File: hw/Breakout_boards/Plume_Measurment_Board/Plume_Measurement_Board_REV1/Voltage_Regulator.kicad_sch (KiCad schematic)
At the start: 0 parts

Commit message: Added Micro-Lock Connectors
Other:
- note added: "5V Voltage Regulator"
- note added: "LMP7721"
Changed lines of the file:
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@@
 	(generator_version "10.0")
 	(paper "A4")
+	(rectangle
+		(start 15.24 15.24)
+		(end 143.51 106.68)
+		(stroke
+			(width 0)
+			(type dash)
+		)
+		(fill
+			(type none)
+		)
+	)
+	(text "LMP7721\n"
+		(exclude_from_sim no)
+		(at 25.0662 22.5284 0)
+		(effects
+			(font
+				(size 2.286 2.286)
+			)
+		)
+	)
+	(text "5V Voltage Regulator"
+		(exclude_from_sim no)
+		(at 17.018 19.812 0)
+		(effects
+			(font
+				(size 2 2)
+				(thickness 0.4)
+				(bold yes)
+			)
+			(justify left bottom)
+		)
+	)
 )

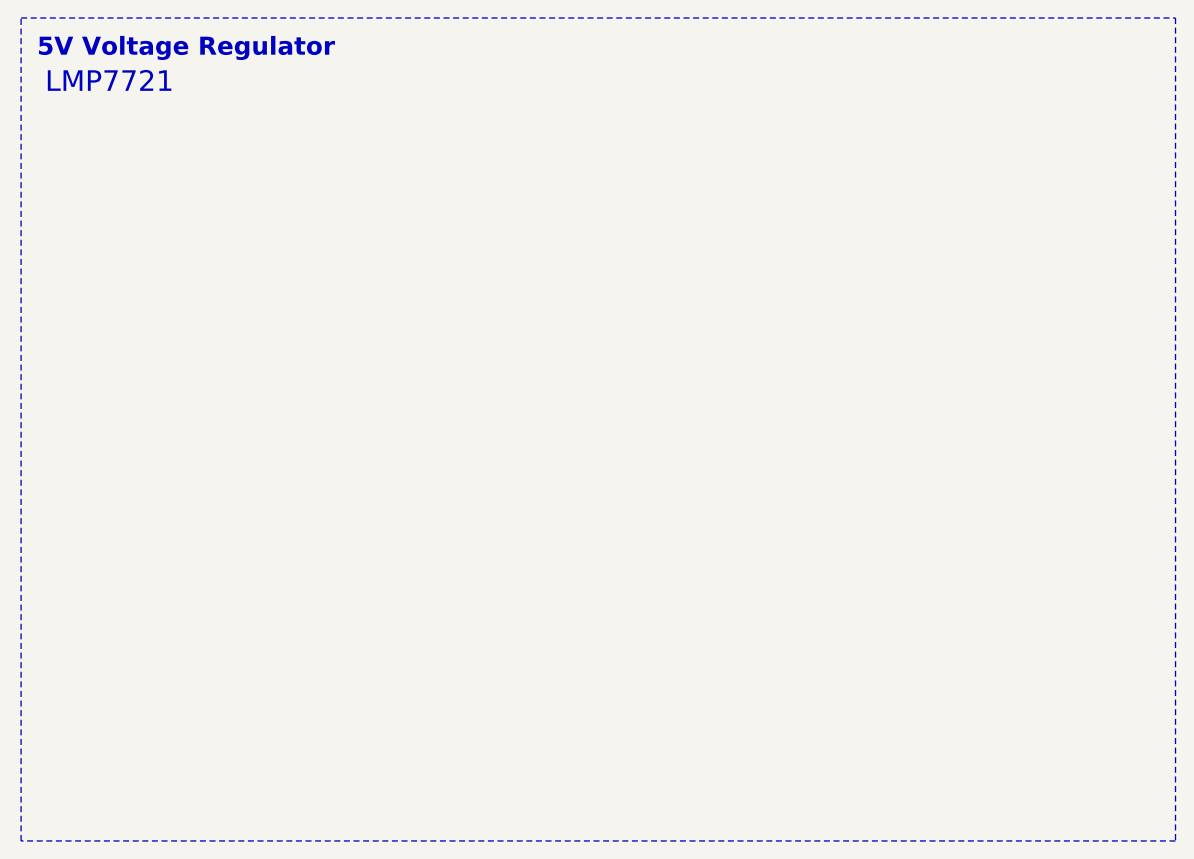
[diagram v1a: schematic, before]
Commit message: Voltage Regulator Library Import + Connector Additions
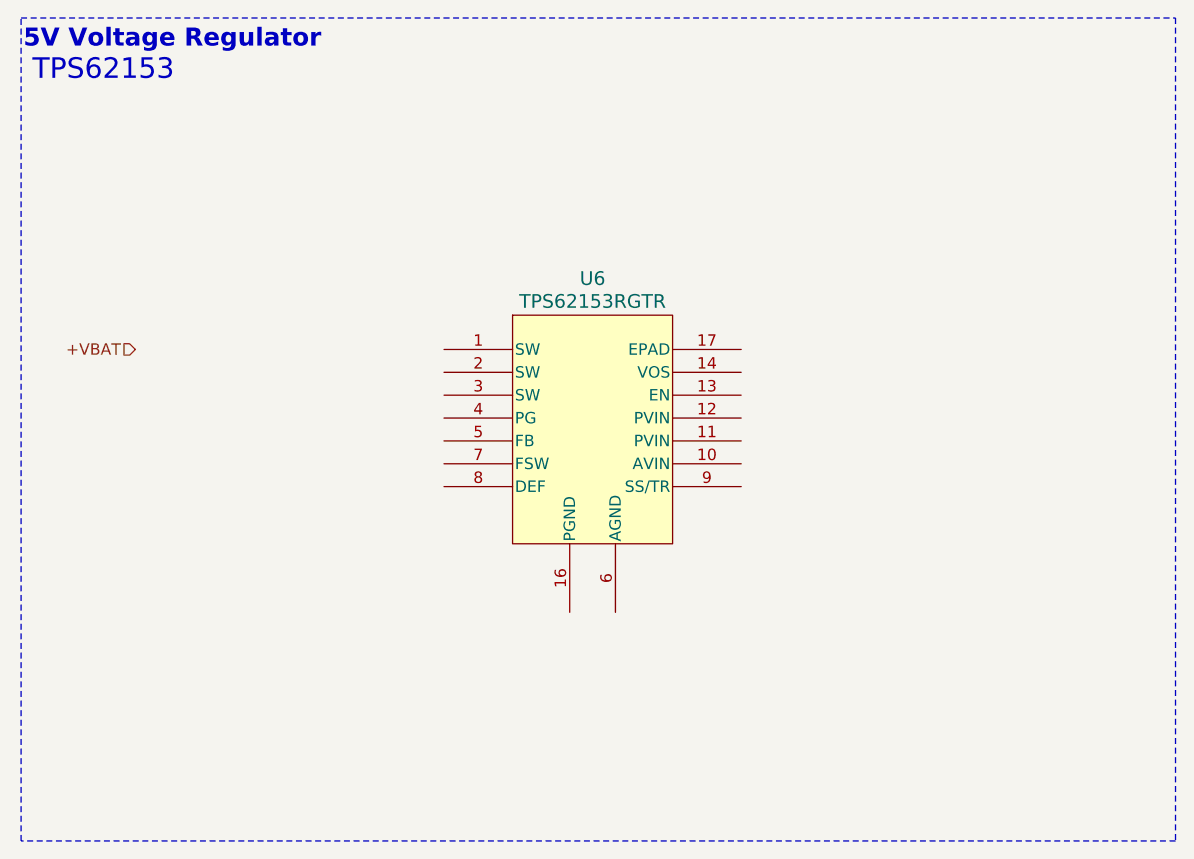
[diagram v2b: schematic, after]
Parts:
- added U6: TPS62153RGTR, RGT16_1P7X1P7, symbol Voltage_Regulator_Texas_Instruments:TPS62153RGTR
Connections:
- new net: U6.15 (PGND), U6.16 (PGND)
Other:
- note added: "TPS62153"
- note removed: "LMP7721"
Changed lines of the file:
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@@
 		)
 	)
-	(text "LMP7721\n"
+	(text "TPS62153\n"
 		(exclude_from_sim no)
-		(at 25.0662 22.5284 0)
+		(at 24.384 21.082 0)
 		(effects
 			(font
@@
 	(text "5V Voltage Regulator"
 		(exclude_from_sim no)
-		(at 17.018 19.812 0)
+		(at 15.494 18.796 0)
 		(effects
 			(font
@@
 		)
 	)
+	(hierarchical_label "+VBAT"
+		(shape input)
+		(at 27.94 52.07 180)
+		(effects
+			(font
+				(size 1.27 1.27)
+			)
+			(justify right)
+		)
+	)
+	(symbol
+		(lib_id "Voltage_Regulator_Texas_Instruments:TPS62153RGTR")
+		(at 48.26 50.8 0)
+		(unit 1)
+		(body_style 1)
+		(exclude_from_sim no)
+		(in_bom yes)
+		(on_board yes)
+		(in_pos_files yes)
+		(dnp no)
+		(property "Reference" "U6"
+			(at 78.74 44.196 0)
+			(show_name no)
+			(do_not_autoplace no)
+			(effects
+				(font
+					(size 1.524 1.524)
+				)
+			)
+		)
+		(property "Value" "TPS62153RGTR"
+			(at 78.74 46.736 0)
+			(show_name no)
+			(do_not_autoplace no)
+			(effects
+				(font
+					(size 1.524 1.524)
+				)
+			)
+		)
+		(property "Footprint" "RGT16_1P7X1P7"
+			(at 48.26 50.8 0)
+			(hide yes)
+			(show_name no)
+			(do_not_autoplace no)
+			(effects
+				(font
+					(size 1.27 1.27)
+					(italic yes)
+				)
+			)
+		)
+		(property "Datasheet" "https://www.ti.com/lit/gpn/tps62153"
+			(at 48.26 50.8 0)
+			(hide yes)
+			(show_name no)
+			(do_not_autoplace no)
+			(effects
+				(font
+					(size 1.27 1.27)
+					(italic yes)
+				)
+			)
+		)
+		(property "Description" ""
+			(at 48.26 50.8 0)
+			(hide yes)
+			(show_name no)
+			(do_not_autoplace no)
+			(effects
+				(font
+					(size 1.27 1.27)
+				)
+			)
+		)
+		(pin "12"
+		)
+		(pin "5"
+		)
+		(pin "9"
+		)
+		(pin "2"
+		)
+		(pin "8"
+		)
+		(pin "6"
+		)
+		(pin "14"
+		)
+		(pin "13"
+		)
+		(pin "15"
+		)
+		(pin "4"
+		)
+		(pin "7"
+		)
+		(pin "16"
+		)
+		(pin "17"
+		)
+		(pin "1"
+		)
+		(pin "3"
+		)
+		(pin "10"
+		)
+		(pin "11"
+		)
+		(instances
+			(project "Plume_Measurment_Board"
+				(path "/2e1d3673-27b9-4604-80fb-036cec98a912/51fb0d9e-13dd-4646-9739-03c7f4c08998"
+					(reference "U6")
+					(unit 1)
+				)
+			)
+		)
+	)

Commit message: 5V Voltage Regulator Addition
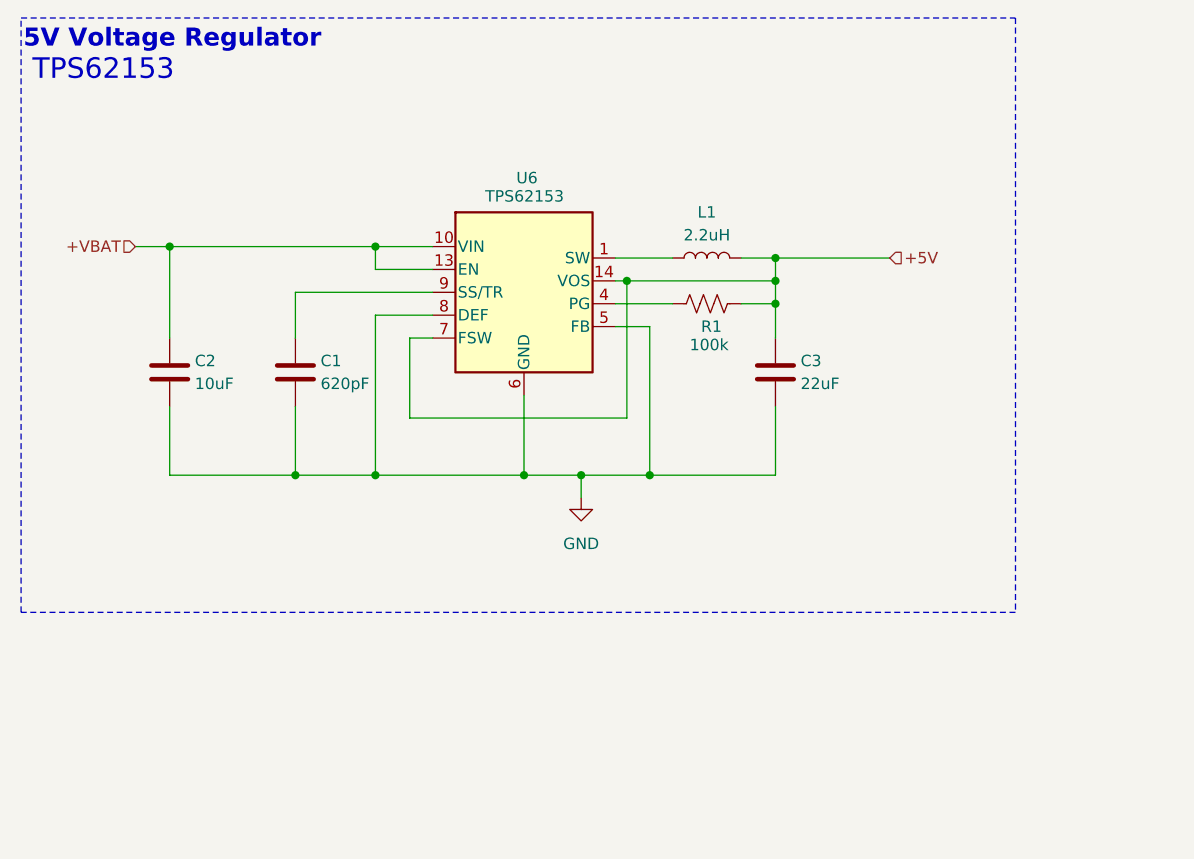
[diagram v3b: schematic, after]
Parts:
- removed U6: TPS62153RGTR, RGT16_1P7X1P7, symbol Voltage_Regulator_Texas_Instruments:TPS62153RGTR
- added C1: 620pF, Capacitor_SMD:C_0402_1005Metric_Pad0.74x0.62mm_HandSolder, symbol Device:C
- added C2: 10uF, Capacitor_SMD:C_0805_2012Metric_Pad1.18x1.45mm_HandSolder, symbol Device:C
- added C3: 22uF, Capacitor_SMD:C_0805_2012Metric_Pad1.18x1.45mm_HandSolder, symbol Device:C
- added L1: 2.2uH, Inductor_TDK:IND_VLS3012CX-2R2M-1, symbol Device:L
- added R1: 100k, symbol Device:R_US
- added U6: TPS62153, Package_DFN_QFN:VQFN-16-1EP_3x3mm_P0.5mm_EP1.68x1.68mm_ThermalVias, symbol Regulator_Switching:TPS62153
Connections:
- net +VBAT: now also C2.1, U6.10 (VIN), U6.11 (VIN), U6.12 (VIN), U6.13 (EN)
- new net: R1.1, U6.4 (PG)
- new net: C1.1, U6.9 (SS/TR)
- new net: L1.1, U6.1 (SW), U6.2 (SW), U6.3 (SW)
- new net +5V: C3.1, L1.2, R1.2, U6.14 (VOS), U6.7 (FSW)
- new net GND: C1.2, C2.2, C3.2, U6.15 (GND), U6.16 (GND), U6.17 (GND), U6.5 (FB), U6.6 (GND), U6.8 (DEF)

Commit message: Connector Fixes
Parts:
- R1: footprint (none) -> Resistor_SMD:R_01005_0402Metric_Pad0.57x0.30mm_HandSolder
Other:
- company: (none) -> Electric Propulsion Lab
- title: (none) -> Plume Measurement Board
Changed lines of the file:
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@@
 	(generator_version "10.0")
 	(paper "A4")
+	(title_block
+		(title "Plume Measurement Board")
+		(date "2026-08-06")
+		(rev "REV1")
+		(company "Electric Propulsion Lab")
+		(comment 4 "Kacper Paraniuk")
+	)
 	(rectangle
 		(start 15.24 15.24)
@@
 	)
 	(junction
+		(at 54.61 40.64)
+		(diameter 0)
+		(color 0 0 0 0)
+	)
+	(junction
+		(at 99.06 46.99)
+		(diameter 0)
+		(color 0 0 0 0)
+	)
+	(junction
 		(at 99.06 41.91)
 		(diameter 0)
@@
 	)
 	(junction
-		(at 54.61 40.64)
-		(diameter 0)
-		(color 0 0 0 0)
-	)
-	(junction
-		(at 99.06 46.99)
-		(diameter 0)
-		(color 0 0 0 0)
-	)
-	(junction
 		(at 82.55 44.45)
 		(diameter 0)
@@
 	(wire
 		(pts
+			(xy 99.06 41.91) (xy 115.57 41.91)
+		)
+		(stroke
+			(width 0)
+			(type default)
+		)
+	)
+	(wire
+		(pts
 			(xy 60.96 48.26) (xy 54.61 48.26)
 		)
@@
 	(wire
 		(pts
-			(xy 99.06 41.91) (xy 111.76 41.91)
-		)
-		(stroke
-			(width 0)
-			(type default)
-		)
-	)
-	(wire
-		(pts
 			(xy 99.06 46.99) (xy 99.06 50.8)
 		)
@@
 	(wire
 		(pts
+			(xy 115.57 41.91) (xy 115.57 38.1)
+		)
+		(stroke
+			(width 0)
+			(type default)
+		)
+	)
+	(wire
+		(pts
 			(xy 54.61 40.64) (xy 60.96 40.64)
 		)
@@
 			(width 0)
 			(type default)
-		)
-	)
-	(hierarchical_label "+5V"
-		(shape input)
-		(at 111.76 41.91 0)
-		(effects
-			(font
-				(size 1.27 1.27)
-			)
-			(justify left)
 		)
 	)
@@
 			)
 		)
-		(property "Footprint" ""
+		(property "Footprint" "Resistor_SMD:R_01005_0402Metric_Pad0.57x0.30mm_HandSolder"
 			(at 91.694 45.974 90)
 			(hide yes)
@@
 			)
 		)
-		(property "Datasheet" ""
+		(property "Datasheet" "https://www.digikey.com/en/products/detail/vishay-dale/CRCW0402100KFKED/1178235?msockid=204984925ffe6bb7012893f25e556a13"
 			(at 91.44 46.99 0)
 			(hide yes)
@@
 					(unit 1)
 				)
+			)
+		)
+	)
+	(symbol
+		(lib_id "power:+3V3")
+		(at 115.57 38.1 0)
+		(unit 1)
+		(body_style 1)
+		(exclude_from_sim no)
+		(in_bom yes)
+		(on_board yes)
+		(in_pos_files yes)
+		(dnp no)
+		(fields_autoplaced yes)
+		(property "Reference" "#PWR0245"
+			(at 115.57 41.91 0)
+			(hide yes)
+			(show_name no)
+			(do_not_autoplace no)
+			(effects
+				(font
+					(size 1.27 1.27)
+				)
+			)
+		)
+		(property "Value" "+5V"
+			(at 115.57 33.02 0)
+			(show_name no)
+			(do_not_autoplace no)
+			(effects
+				(font
+					(size 1.27 1.27)
+				)
+			)
+		)
+		(property "Footprint" ""
+			(at 115.57 38.1 0)
+			(hide yes)
+			(show_name no)
+			(do_not_autoplace no)
+			(effects
+				(font
+					(size 1.27 1.27)
+				)
+			)
+		)
+		(property "Datasheet" ""
+			(at 115.57 38.1 0)
+			(hide yes)
+			(show_name no)
+			(do_not_autoplace no)
+			(effects
+				(font
+					(size 1.27 1.27)
+				)
+			)
+		)
+		(property "Description" "Power symbol creates a global label with name \"+3V3\""
+			(at 115.57 38.1 0)
+			(hide yes)
+			(show_name no)
+			(do_not_autoplace no)
+			(effects
+				(font
+					(size 1.27 1.27)
+				)
+			)
+		)
+		(pin "1"
+		)
+		(instances
+			(project "Plume_Measurment_Board"
+				(path "/2e1d3673-27b9-4604-80fb-036cec98a912/51fb0d9e-13dd-4646-9739-03c7f4c08998"
+					(reference "#PWR0245")
+					(unit 1)
+				)
